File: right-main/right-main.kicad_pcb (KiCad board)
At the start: 2 copper layers, 150.4 x 123.8 mm, 209 parts, among them J1 USBCONN, P1 CONN_4, P2 CONN_5, P3 CONN_6, SW1 PTS525SM10, SW11 SPST, SW12 SPST, SW13 SPST, SW14 SPST, SW15 SPST, SW16 SPST, SW17 SPST, SW21 SPST, SW22 SPST, SW23 SPST, SW24 SPST, SW25 SPST, SW26 SPST, SW27 SPST, SW31 SPST, SW32 SPST, SW33 SPST, SW34 SPST, SW35 SPST, SW36 SPST, SW37 SPST, SW41 SPST, SW42 SPST, SW43 SPST, SW44 SPST, SW45 SPST, SW46 SPST, SW47 SPST, SW52 SPST, SW53 SPST, SW54 SPST, SW55 SPST, SW56 SPST, SW57 SPST, U1 ATMEGA32U4, U2 CAT24C256, X1 16Mhz

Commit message: switch 44 right
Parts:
- SW44: footprint UGL:Cherry_MX -> ugl:Cherry-MX-Matias-Hybrid
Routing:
- net Net-(D44-Pad2): track 7.10 -> 9.10 mm
- net /ROW4: track 218.3 -> 219.1 mm
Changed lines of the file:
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@@
 (kicad_pcb (version 4) (host pcbnew 4.0.1-stable)
   (general
-    (links 355)
+    (links 357)
     (no_connects 0)
     (area 19.803 18.9051 270.000001 165.000001)
     (thickness 1.6)
     (drawings 354)
-    (tracks 1076)
+    (tracks 1084)
     (zones 0)
     (modules 209)
@@
       (net 19 /ROW4))
   )
-  (module UGL:Cherry_MX locked (layer F.Cu)
-    (at 168.54 120.7 180)
-    (fp_text reference SW44 (at 0 4.9 180) (layer F.SilkS)
-      (effects (font (size 1.5 1.5) (thickness 0.3)))
-    )
-    (fp_text value SPST (at 0 0 180) (layer F.SilkS) hide
-      (effects (font (size 1.5 1.5) (thickness 0.3)))
-    )
-    (fp_line (start -7.6 -7.6) (end -7.6 7.6) (layer B.SilkS) (width 0.15))
-    (fp_line (start -7.6 7.6) (end 7.6 7.6) (layer B.SilkS) (width 0.15))
-    (fp_line (start 7.6 -7.6) (end 7.6 7.6) (layer B.SilkS) (width 0.15))
-    (fp_line (start -7.6 -7.6) (end 7.6 -7.6) (layer B.SilkS) (width 0.15))
-    (fp_line (start -7.62 -7.62) (end 7.62 -7.62) (layer F.SilkS) (width 0.15))
-    (fp_line (start 7.62 -7.62) (end 7.62 7.62) (layer F.SilkS) (width 0.15))
-    (fp_line (start 7.62 7.62) (end -7.62 7.62) (layer F.SilkS) (width 0.15))
-    (fp_line (start -7.62 7.62) (end -7.62 -7.62) (layer F.SilkS) (width 0.15))
-    (pad "" np_thru_hole circle (at 0 0 180) (size 4 4) (drill 4) (layers *.Cu *.Mask F.SilkS))
-    (pad 2 thru_hole circle (at -3.81 -2.54 180) (size 2.5 2.5) (drill 1.5) (layers *.Cu *.Mask F.SilkS)
-      (net 54 "Net-(D44-Pad2)"))
-    (pad 1 thru_hole circle (at 2.54 -5.08 180) (size 2.5 2.5) (drill 1.5) (layers *.Cu *.Mask F.SilkS)
-      (net 19 /ROW4))
-  )
   (module UGL:UX60-MB-5S8 locked (layer F.Cu)
     (at 175.849803 43.601924 85.4)
@@
       (net 27 GND) (solder_mask_margin -1))
   )
+  (module ugl:Cherry-MX-Matias-Hybrid locked (layer F.Cu)
+    (at 168.54 120.7 180)
+    (tags switch)
+    (fp_text reference SW44 (at 0 3.81 180) (layer F.SilkS)
+      (effects (font (thickness 0.3048)))
+    )
+    (fp_text value SPST (at 0 0 180) (layer F.SilkS) hide
+      (effects (font (thickness 0.3048)))
+    )
+    (fp_line (start -7.62 7.62) (end -7.62 -7.62) (layer B.SilkS) (width 0.15))
+    (fp_line (start 7.62 7.62) (end -7.62 7.62) (layer B.SilkS) (width 0.15))
+    (fp_line (start 7.62 -7.62) (end 7.62 7.62) (layer B.SilkS) (width 0.15))
+    (fp_line (start -7.62 -7.62) (end 7.62 -7.62) (layer B.SilkS) (width 0.15))
+    (fp_line (start -7.75 -6.4) (end -7.75 6.4) (layer F.SilkS) (width 0.15))
+    (fp_line (start 7.75 -6.4) (end 7.75 6.4) (layer F.SilkS) (width 0.15))
+    (fp_line (start -7.75 6.4) (end 7.75 6.4) (layer F.SilkS) (width 0.15))
+    (fp_line (start -7.75 -6.4) (end 7.75 -6.4) (layer F.SilkS) (width 0.15))
+    (fp_line (start -7.62 -7.62) (end 7.62 -7.62) (layer F.SilkS) (width 0.15))
+    (fp_line (start 7.62 -7.62) (end 7.62 7.62) (layer F.SilkS) (width 0.15))
+    (fp_line (start 7.62 7.62) (end -7.62 7.62) (layer F.SilkS) (width 0.15))
+    (fp_line (start -7.62 7.62) (end -7.62 -7.62) (layer F.SilkS) (width 0.15))
+    (pad 0 thru_hole circle (at 0 0 180) (size 3.98018 3.98018) (drill 3.98018) (layers *.Cu *.Mask F.SilkS))
+    (pad 1 thru_hole circle (at 2.54 -5.08 180) (size 2.6 2.6) (drill 1.5011) (layers *.Cu *.Mask F.SilkS)
+      (net 19 /ROW4))
+    (pad 2 thru_hole circle (at -3.81 -2.54 180) (size 2.6 2.6) (drill 1.5011) (layers *.Cu *.Mask F.SilkS)
+      (net 54 "Net-(D44-Pad2)"))
+    (pad "" thru_hole circle (at -5.08 0 180) (size 1.69926 1.69926) (drill 1.69926) (layers *.Cu *.Mask F.SilkS))
+    (pad "" thru_hole circle (at 5.08 0 180) (size 1.69926 1.69926) (drill 1.69926) (layers *.Cu *.Mask F.SilkS))
+    (pad 1 thru_hole circle (at 2.5 -4.5 180) (size 2.5 2.5) (drill 1.5) (layers *.Cu *.Mask F.SilkS)
+      (net 19 /ROW4))
+    (pad 2 thru_hole circle (at -2.5 -4 180) (size 2.5 2.5) (drill 1.5) (layers *.Cu *.Mask F.SilkS)
+      (net 54 "Net-(D44-Pad2)"))
+    (model cherry_mx1.wrl
+      (at (xyz 0 0 0))
+      (scale (xyz 1 1 1))
+      (rotate (xyz 0 0 0))
+    )
+  )
   (gr_line (start 120.857 138.196) (end 121.657 137.396) (angle 90) (layer B.SilkS) (width 0.2))
   (gr_line (start 124.457 148.096) (end 124.457 148.296) (angle 90) (layer B.SilkS) (width 0.2))
@@
   (segment (start 151.0203 126.4513) (end 151.0203 130.396) (width 0.4064) (layer B.Cu) (net 2))
   (segment (start 149.7945 111.1504) (end 149.7945 115.4585) (width 0.4064) (layer B.Cu) (net 2))
+  (segment (start 174.3203 111.196) (end 174.3203 111.2234) (width 0.4064) (layer B.Cu) (net 3))
+  (segment (start 174.3203 111.2234) (end 164.716031 120.827669) (width 0.4064) (layer B.Cu) (net 3))
+  (segment (start 164.716031 120.827669) (end 164.716031 124.072495) (width 0.4064) (layer B.Cu) (net 3))
+  (segment (start 164.716031 124.072495) (end 164.1203 124.668226) (width 0.4064) (layer B.Cu) (net 3))
+  (segment (start 164.1203 124.668226) (end 164.1203 129.18) (width 0.4064) (layer B.Cu) (net 3))
+  (segment (start 164.1203 129.18) (end 164.1203 130.196) (width 0.4064) (layer B.Cu) (net 3))
   (segment (start 184.5203 92.196) (end 183.5317 92.196) (width 0.4064) (layer B.Cu) (net 3))
   (segment (start 183.5317 92.196) (end 174.606034 101.121666) (width 0.4064) (layer B.Cu) (net 3))
@@
   (segment (start 164.1203 130.196) (end 164.1203 131.494808) (width 0.4064) (layer B.Cu) (net 3))
   (segment (start 173.957 110.8327) (end 174.3203 111.196) (width 0.4064) (layer B.Cu) (net 3))
-  (segment (start 173.557 111.196) (end 164.1203 120.6327) (width 0.4064) (layer B.Cu) (net 3))
-  (segment (start 164.1203 120.6327) (end 164.1203 130.196) (width 0.4064) (layer B.Cu) (net 3))
-  (segment (start 174.3203 111.196) (end 173.557 111.196) (width 0.4064) (layer B.Cu) (net 3))
   (segment (start 198.536031 87.764269) (end 198.536031 82.097104) (width 0.4064) (layer B.Cu) (net 4))
   (segment (start 183.8203 73.196) (end 187.257 73.196) (width 0.4064) (layer B.Cu) (net 4))
@@
   (segment (start 207.6977 115.8367) (end 218.028 115.8367) (width 0.4064) (layer B.Cu) (net 18))
   (segment (start 214.07 106.78) (end 209.997216 106.78) (width 0.4064) (layer B.Cu) (net 18))
+  (segment (start 184.92 125.78) (end 183.152234 125.78) (width 0.4064) (layer F.Cu) (net 19))
+  (segment (start 181.852235 127.079999) (end 167.299999 127.079999) (width 0.4064) (layer F.Cu) (net 19))
+  (segment (start 183.152234 125.78) (end 181.852235 127.079999) (width 0.4064) (layer F.Cu) (net 19))
+  (segment (start 167.299999 127.079999) (end 166 125.78) (width 0.4064) (layer F.Cu) (net 19))
   (segment (start 166 125.78) (end 164.232234 125.78) (width 0.4064) (layer F.Cu) (net 19))
   (segment (start 164.232234 125.78) (end 162.932235 127.079999) (width 0.4064) (layer F.Cu) (net 19))
@@
   (segment (start 203.357 125.297) (end 203.84 125.78) (width 0.4064) (layer B.Cu) (net 19))
   (segment (start 204.959999 125.78) (end 185.759998 125.78) (width 0.4064) (layer F.Cu) (net 19))
-  (segment (start 185.759998 125.78) (end 166.560002 125.78) (width 0.4064) (layer F.Cu) (net 19))
   (segment (start 218.028 117.4369) (end 217.064617 117.4369) (width 0.4064) (layer B.Cu) (net 19))
   (segment (start 206.103 117.4369) (end 218.028 117.4369) (width 0.4064) (layer B.Cu) (net 19))
@@
   (segment (start 153.43 123.24) (end 153.6377 123.24) (width 0.4064) (layer B.Cu) (net 53))
   (segment (start 153.6377 123.24) (end 160.5937 130.196) (width 0.4064) (layer B.Cu) (net 53))
+  (segment (start 171.04 124.7) (end 171.04 124.55) (width 0.4064) (layer B.Cu) (net 54))
+  (segment (start 171.04 124.55) (end 172.35 123.24) (width 0.4064) (layer B.Cu) (net 54))
   (segment (start 172.35 129.8523) (end 172.6937 130.196) (width 0.4064) (layer B.Cu) (net 54))
   (segment (start 172.35 123.24) (end 172.35 129.8523) (width 0.4064) (layer B.Cu) (net 54))

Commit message: switch 45 right
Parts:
- SW45: footprint UGL:Cherry_MX -> ugl:Cherry-MX-Matias-Hybrid
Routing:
- net Net-(D45-Pad2): track 9.68 -> 11.7 mm
- net /ROW4: track 219.1 -> 219.9 mm
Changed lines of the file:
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@@
 (kicad_pcb (version 4) (host pcbnew 4.0.1-stable)
   (general
-    (links 357)
-    (no_connects 0)
+    (links 359)
+    (no_connects 1)
     (area 19.803 18.9051 270.000001 165.000001)
     (thickness 1.6)
     (drawings 354)
-    (tracks 1084)
+    (tracks 1089)
     (zones 0)
     (modules 209)
@@
   )
   (layers
-    (0 F.Cu signal hide)
-    (31 B.Cu signal)
+    (0 F.Cu signal)
+    (31 B.Cu signal hide)
     (32 B.Adhes user)
     (33 F.Adhes user)
@@
       (net 19 /ROW4))
   )
-  (module UGL:Cherry_MX locked (layer F.Cu)
-    (at 187.46 120.7 180)
-    (fp_text reference SW45 (at 0 4.9 180) (layer F.SilkS)
-      (effects (font (size 1.5 1.5) (thickness 0.3)))
-    )
-    (fp_text value SPST (at 0 0 180) (layer F.SilkS) hide
-      (effects (font (size 1.5 1.5) (thickness 0.3)))
-    )
-    (fp_line (start -7.6 -7.6) (end -7.6 7.6) (layer B.SilkS) (width 0.15))
-    (fp_line (start -7.6 7.6) (end 7.6 7.6) (layer B.SilkS) (width 0.15))
-    (fp_line (start 7.6 -7.6) (end 7.6 7.6) (layer B.SilkS) (width 0.15))
-    (fp_line (start -7.6 -7.6) (end 7.6 -7.6) (layer B.SilkS) (width 0.15))
-    (fp_line (start -7.62 -7.62) (end 7.62 -7.62) (layer F.SilkS) (width 0.15))
-    (fp_line (start 7.62 -7.62) (end 7.62 7.62) (layer F.SilkS) (width 0.15))
-    (fp_line (start 7.62 7.62) (end -7.62 7.62) (layer F.SilkS) (width 0.15))
-    (fp_line (start -7.62 7.62) (end -7.62 -7.62) (layer F.SilkS) (width 0.15))
-    (pad "" np_thru_hole circle (at 0 0 180) (size 4 4) (drill 4) (layers *.Cu *.Mask F.SilkS))
-    (pad 2 thru_hole circle (at -3.81 -2.54 180) (size 2.5 2.5) (drill 1.5) (layers *.Cu *.Mask F.SilkS)
-      (net 55 "Net-(D45-Pad2)"))
-    (pad 1 thru_hole circle (at 2.54 -5.08 180) (size 2.5 2.5) (drill 1.5) (layers *.Cu *.Mask F.SilkS)
-      (net 19 /ROW4))
-  )
   (module UGL:UX60-MB-5S8 locked (layer F.Cu)
     (at 175.849803 43.601924 85.4)
@@
     )
   )
+  (module ugl:Cherry-MX-Matias-Hybrid locked (layer F.Cu)
+    (at 187.46 120.7 180)
+    (tags switch)
+    (fp_text reference SW45 (at 0 3.81 180) (layer F.SilkS)
+      (effects (font (thickness 0.3048)))
+    )
+    (fp_text value SPST (at 0 0 180) (layer F.SilkS) hide
+      (effects (font (thickness 0.3048)))
+    )
+    (fp_line (start -7.62 7.62) (end -7.62 -7.62) (layer B.SilkS) (width 0.15))
+    (fp_line (start 7.62 7.62) (end -7.62 7.62) (layer B.SilkS) (width 0.15))
+    (fp_line (start 7.62 -7.62) (end 7.62 7.62) (layer B.SilkS) (width 0.15))
+    (fp_line (start -7.62 -7.62) (end 7.62 -7.62) (layer B.SilkS) (width 0.15))
+    (fp_line (start -7.75 -6.4) (end -7.75 6.4) (layer F.SilkS) (width 0.15))
+    (fp_line (start 7.75 -6.4) (end 7.75 6.4) (layer F.SilkS) (width 0.15))
+    (fp_line (start -7.75 6.4) (end 7.75 6.4) (layer F.SilkS) (width 0.15))
+    (fp_line (start -7.75 -6.4) (end 7.75 -6.4) (layer F.SilkS) (width 0.15))
+    (fp_line (start -7.62 -7.62) (end 7.62 -7.62) (layer F.SilkS) (width 0.15))
+    (fp_line (start 7.62 -7.62) (end 7.62 7.62) (layer F.SilkS) (width 0.15))
+    (fp_line (start 7.62 7.62) (end -7.62 7.62) (layer F.SilkS) (width 0.15))
+    (fp_line (start -7.62 7.62) (end -7.62 -7.62) (layer F.SilkS) (width 0.15))
+    (pad 0 thru_hole circle (at 0 0 180) (size 3.98018 3.98018) (drill 3.98018) (layers *.Cu *.Mask F.SilkS))
+    (pad 1 thru_hole circle (at 2.54 -5.08 180) (size 2.6 2.6) (drill 1.5011) (layers *.Cu *.Mask F.SilkS)
+      (net 19 /ROW4))
+    (pad 2 thru_hole circle (at -3.81 -2.54 180) (size 2.6 2.6) (drill 1.5011) (layers *.Cu *.Mask F.SilkS)
+      (net 55 "Net-(D45-Pad2)"))
+    (pad "" thru_hole circle (at -5.08 0 180) (size 1.69926 1.69926) (drill 1.69926) (layers *.Cu *.Mask F.SilkS))
+    (pad "" thru_hole circle (at 5.08 0 180) (size 1.69926 1.69926) (drill 1.69926) (layers *.Cu *.Mask F.SilkS))
+    (pad 1 thru_hole circle (at 2.5 -4.5 180) (size 2.5 2.5) (drill 1.5) (layers *.Cu *.Mask F.SilkS)
+      (net 19 /ROW4))
+    (pad 2 thru_hole circle (at -2.5 -4 180) (size 2.5 2.5) (drill 1.5) (layers *.Cu *.Mask F.SilkS)
+      (net 55 "Net-(D45-Pad2)"))
+    (model cherry_mx1.wrl
+      (at (xyz 0 0 0))
+      (scale (xyz 1 1 1))
+      (rotate (xyz 0 0 0))
+    )
+  )
   (gr_line (start 120.857 138.196) (end 121.657 137.396) (angle 90) (layer B.SilkS) (width 0.2))
   (gr_line (start 124.457 148.096) (end 124.457 148.296) (angle 90) (layer B.SilkS) (width 0.2))
@@
   (segment (start 207.6977 115.8367) (end 218.028 115.8367) (width 0.4064) (layer B.Cu) (net 18))
   (segment (start 214.07 106.78) (end 209.997216 106.78) (width 0.4064) (layer B.Cu) (net 18))
+  (segment (start 203.84 125.78) (end 202.072234 125.78) (width 0.4064) (layer F.Cu) (net 19))
+  (segment (start 202.072234 125.78) (end 200.772235 127.079999) (width 0.4064) (layer F.Cu) (net 19))
+  (segment (start 200.772235 127.079999) (end 186.219999 127.079999) (width 0.4064) (layer F.Cu) (net 19))
+  (segment (start 186.219999 127.079999) (end 184.92 125.78) (width 0.4064) (layer F.Cu) (net 19))
   (segment (start 184.92 125.78) (end 183.152234 125.78) (width 0.4064) (layer F.Cu) (net 19))
   (segment (start 181.852235 127.079999) (end 167.299999 127.079999) (width 0.4064) (layer F.Cu) (net 19))
@@
   (segment (start 203.357 119.396) (end 203.357 125.297) (width 0.4064) (layer B.Cu) (net 19))
   (segment (start 203.357 125.297) (end 203.84 125.78) (width 0.4064) (layer B.Cu) (net 19))
-  (segment (start 204.959999 125.78) (end 185.759998 125.78) (width 0.4064) (layer F.Cu) (net 19))
   (segment (start 218.028 117.4369) (end 217.064617 117.4369) (width 0.4064) (layer B.Cu) (net 19))
   (segment (start 206.103 117.4369) (end 218.028 117.4369) (width 0.4064) (layer B.Cu) (net 19))
@@
   (segment (start 172.35 129.8523) (end 172.6937 130.196) (width 0.4064) (layer B.Cu) (net 54))
   (segment (start 172.35 123.24) (end 172.35 129.8523) (width 0.4064) (layer B.Cu) (net 54))
+  (segment (start 189.96 124.7) (end 189.96 124.55) (width 0.4064) (layer B.Cu) (net 55) (status C00000))
+  (segment (start 189.96 124.55) (end 191.27 123.24) (width 0.4064) (layer B.Cu) (net 55) (status C00000))
   (segment (start 191.27 123.6197) (end 191.27 123.24) (width 0.4064) (layer B.Cu) (net 55))
   (segment (start 184.6937 130.196) (end 191.27 123.6197) (width 0.4064) (layer B.Cu) (net 55))

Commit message: switch 46 right
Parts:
- SW46: footprint UGL:Cherry_MX -> ugl:Cherry-MX-Matias-Hybrid
- moved via 38/22mil 0.51 mm to (210.1, 119.4)
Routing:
- net Net-(D46-Pad2): track 9.85 -> 11.9 mm
- net /COL6: track 101.1 -> 102.1 mm
- net /ROW4: track 219.9 -> 220.7 mm
- net /ROW5: track 167.2 -> 166.6 mm
- net /COL4: track 148.0 -> 147.4 mm
- net /COL5: track 126.2 -> 125.6 mm
- net /RX2: track 147.0 -> 146.4 mm

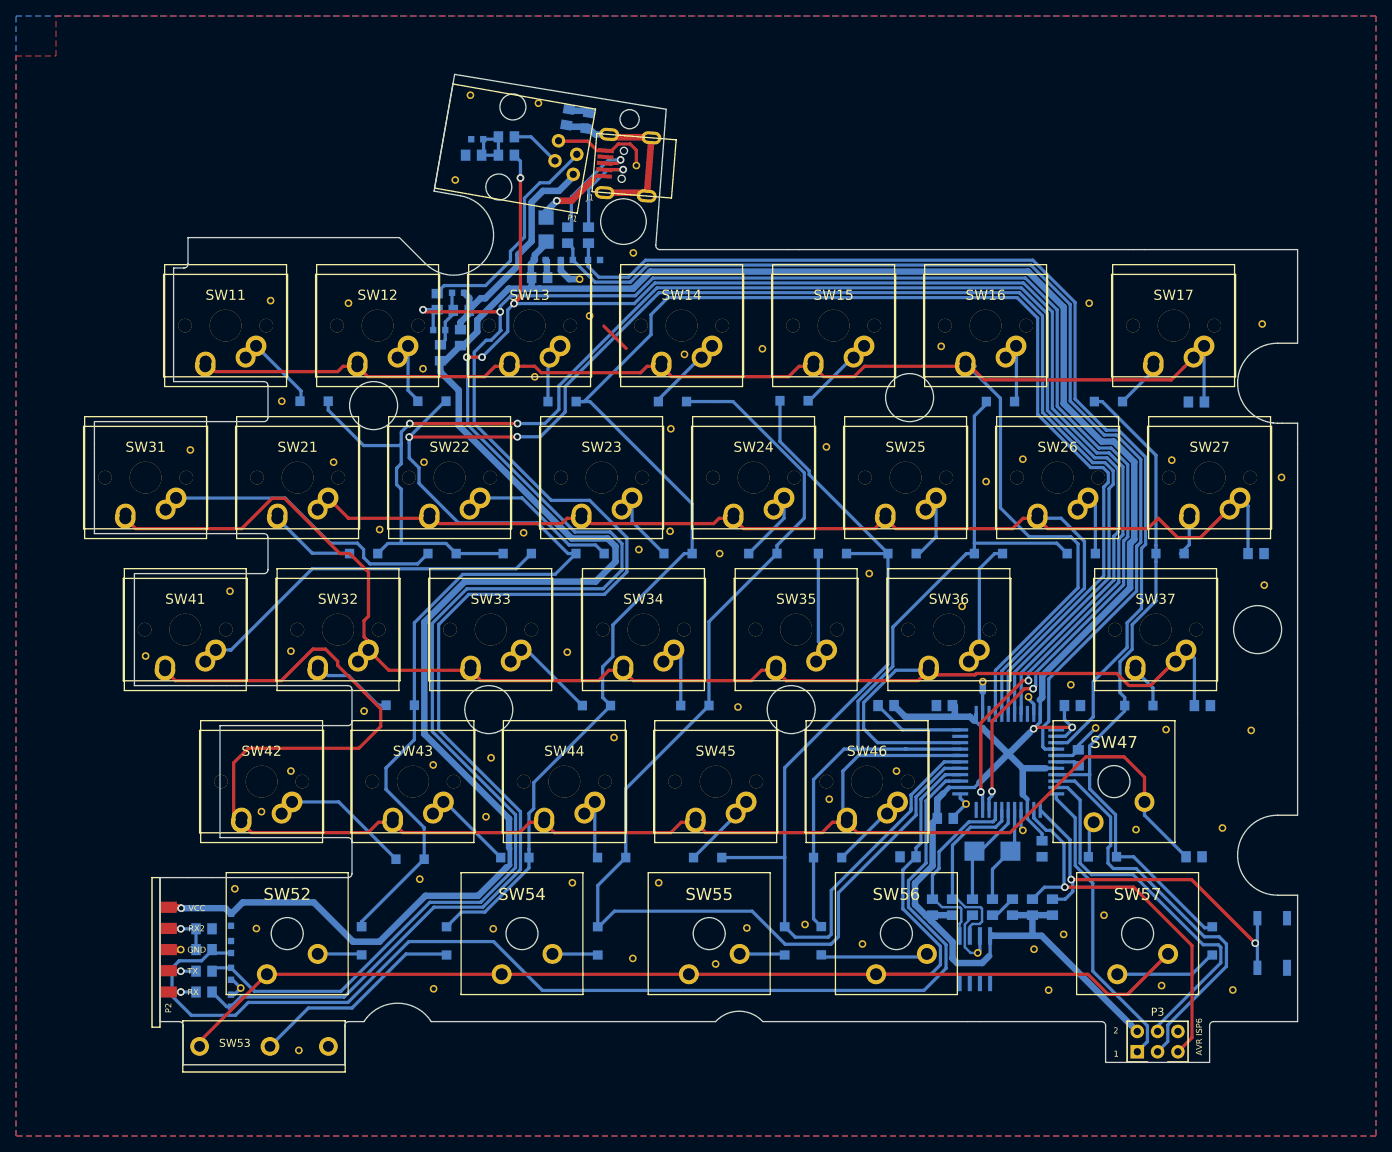
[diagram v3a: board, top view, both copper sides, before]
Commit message: switch 47 right
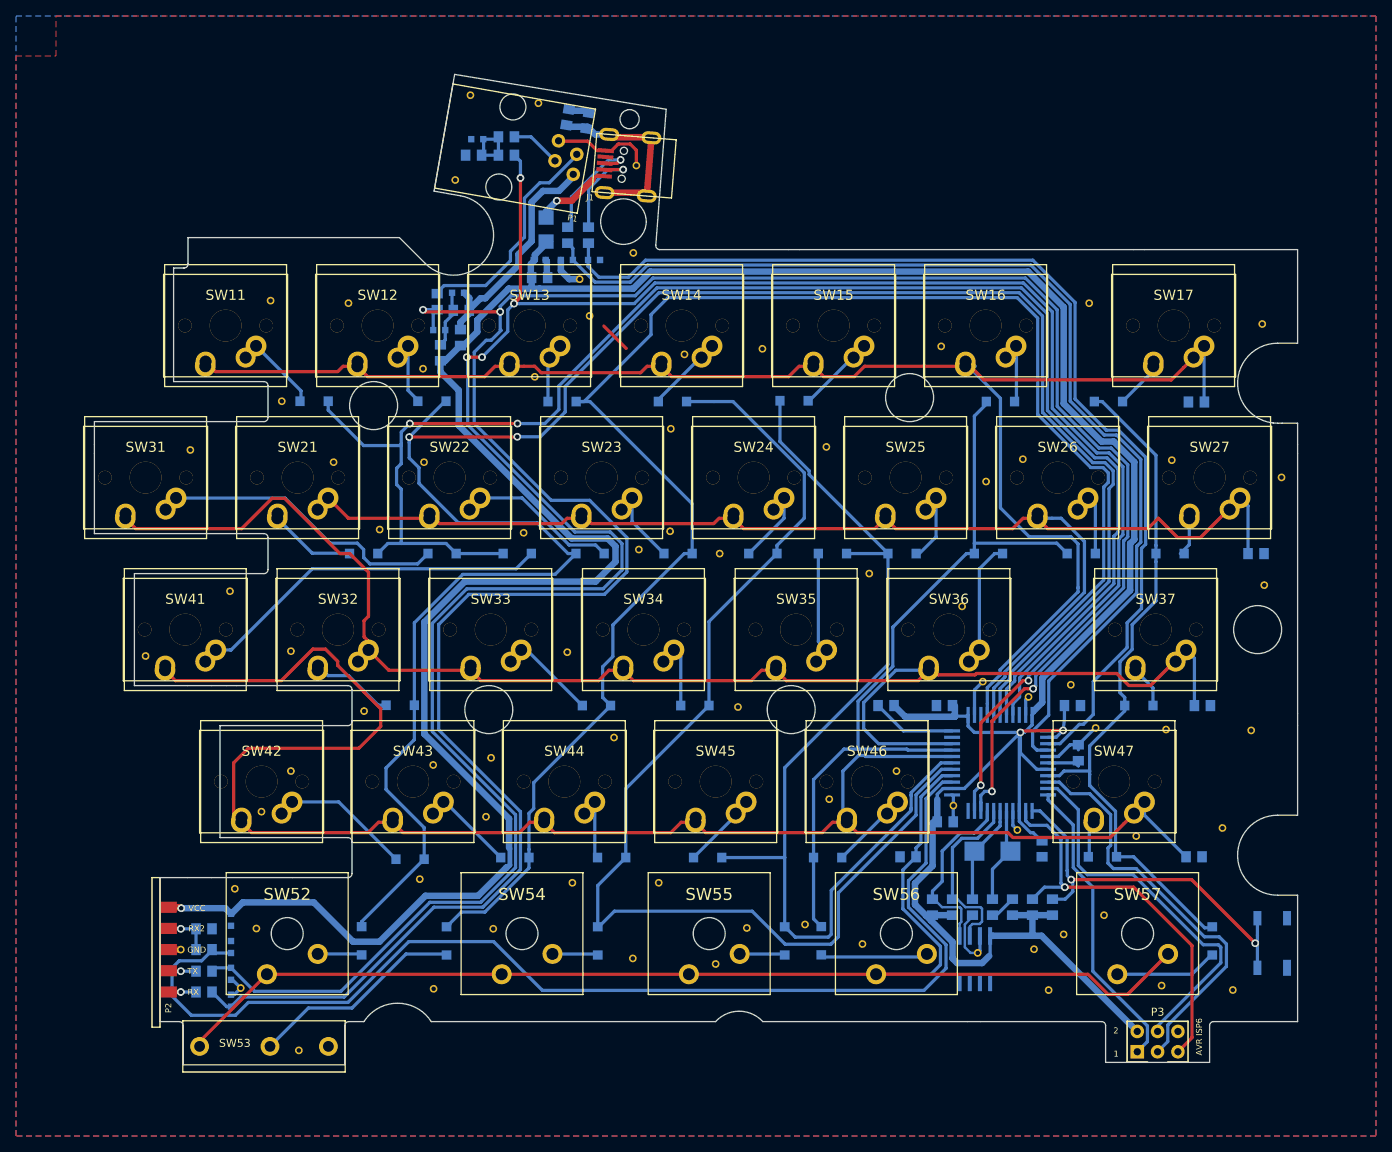
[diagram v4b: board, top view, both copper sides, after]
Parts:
- SW47: footprint UGL:Cherry_MX -> ugl:Cherry-MX-Matias-Hybrid
- moved via 38/22mil 1.60 mm to (217.2, 123.7)
- moved U1 1.02 mm to (223.0, 118.4)
- moved via 38/22mil 0.81 mm to (240.0, 127.5)
- moved via 38/22mil 0.69 mm to (225.2, 126.7)
- moved C5 0.64 mm to (232.8, 117.1)
- moved C4 0.43 mm to (216.2, 125.7)
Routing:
- net /ROW4: track 220.7 -> 213.6 mm
- net VCC: track 435.2 -> 438.8 mm
- net /UCAP: track 3.30 -> 4.92 mm
- net /SDA: track 23.8 -> 22.5 mm
- net /COL7: track 86.5 -> 87.8 mm
- net GND: track 66.0 -> 67.2 mm
- net /SCL: track 24.3 -> 23.1 mm
- net /RESET: track 49.2 -> 50.4 mm
- net /COL6: track 102.1 -> 100.9 mm
- net /SCK: track 50.6 -> 51.7 mm
- net /MISO: track 37.7 -> 38.7 mm
- net /RX: track 315.8 -> 316.8 mm
- net /ROW3: track 191.3 -> 190.4 mm
- net /HWB: track 11.5 -> 10.6 mm
- net /COL4: track 147.4 -> 146.5 mm
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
